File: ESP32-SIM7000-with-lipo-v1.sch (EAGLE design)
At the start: 65 parts, among them IC2 TXB0104, Q1 BSS138L, Q2 BSS138L, Q3 9013, Q5 9013, U3 ESP-WROOM-32, U4 MCP73831T-2ACI/OT, X1 LTE-uFL

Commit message: Naming components
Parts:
- renumbered PGM1 to PROGRAM
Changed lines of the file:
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@@
 <part name="+3V6" library="supply1" library_urn="urn:adsk.eagle:library:371" deviceset="+3V3" device=""/>
 <part name="GND52" library="supply1" library_urn="urn:adsk.eagle:library:371" deviceset="GND" device=""/>
-<part name="PGM1" library="pinhead" deviceset="PINHD-1X6" device=""/>
+<part name="PROGRAM" library="pinhead" deviceset="PINHD-1X6" device=""/>
 <part name="GND3" library="supply1" library_urn="urn:adsk.eagle:library:371" deviceset="GND" device=""/>
 <part name="V2" library="Adafruit111" deviceset="VBUS" device=""/>
@@
 <attribute name="VALUE" x="-78.74" y="-2.54" size="1.778" layer="96"/>
 </instance>
-<instance part="PGM1" gate="A" x="-93.98" y="-63.5" rot="R180">
+<instance part="PROGRAM" gate="A" x="-93.98" y="-63.5" rot="R180">
 <attribute name="NAME" x="-87.63" y="-74.295" size="1.778" layer="95" rot="R180"/>
 <attribute name="VALUE" x="-87.63" y="-53.34" size="1.778" layer="96" rot="R180"/>
@@
 </segment>
 <segment>
-<pinref part="PGM1" gate="A" pin="1"/>
+<pinref part="PROGRAM" gate="A" pin="1"/>
 <wire x1="-91.44" y1="-71.12" x2="-83.82" y2="-71.12" width="0.1524" layer="91"/>
 <pinref part="GND3" gate="1" pin="GND"/>
@@
 </segment>
 <segment>
-<pinref part="PGM1" gate="A" pin="5"/>
+<pinref part="PROGRAM" gate="A" pin="5"/>
 <wire x1="-91.44" y1="-60.96" x2="-78.74" y2="-60.96" width="0.1524" layer="91"/>
 <label x="-78.74" y="-60.96" size="1.27" layer="95" xref="yes"/>
@@
 </segment>
 <segment>
-<pinref part="PGM1" gate="A" pin="6"/>
+<pinref part="PROGRAM" gate="A" pin="6"/>
 <wire x1="-91.44" y1="-58.42" x2="-78.74" y2="-58.42" width="0.1524" layer="91"/>
 <label x="-78.74" y="-58.42" size="1.27" layer="95" xref="yes"/>
@@
 </segment>
 <segment>
-<pinref part="PGM1" gate="A" pin="4"/>
+<pinref part="PROGRAM" gate="A" pin="4"/>
 <wire x1="-91.44" y1="-63.5" x2="-78.74" y2="-63.5" width="0.1524" layer="91"/>
 <label x="-78.74" y="-63.5" size="1.27" layer="95" xref="yes"/>
@@
 </segment>
 <segment>
-<pinref part="PGM1" gate="A" pin="3"/>
+<pinref part="PROGRAM" gate="A" pin="3"/>
 <wire x1="-91.44" y1="-66.04" x2="-78.74" y2="-66.04" width="0.1524" layer="91"/>
 <label x="-78.74" y="-66.04" size="1.27" layer="95" xref="yes"/>
@@
 <net name="VBUS" class="3">
 <segment>
-<pinref part="PGM1" gate="A" pin="2"/>
+<pinref part="PROGRAM" gate="A" pin="2"/>
 <wire x1="-91.44" y1="-68.58" x2="-83.82" y2="-68.58" width="0.1524" layer="91"/>
 <wire x1="-83.82" y1="-68.58" x2="-83.82" y2="-52.07" width="0.1524" layer="91"/>

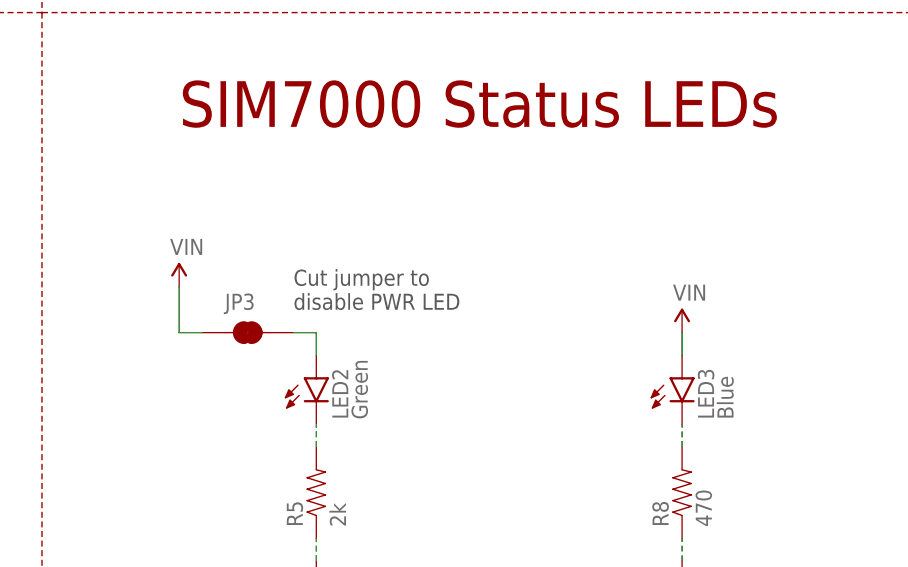
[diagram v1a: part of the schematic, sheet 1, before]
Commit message: adds vias and completes DRC
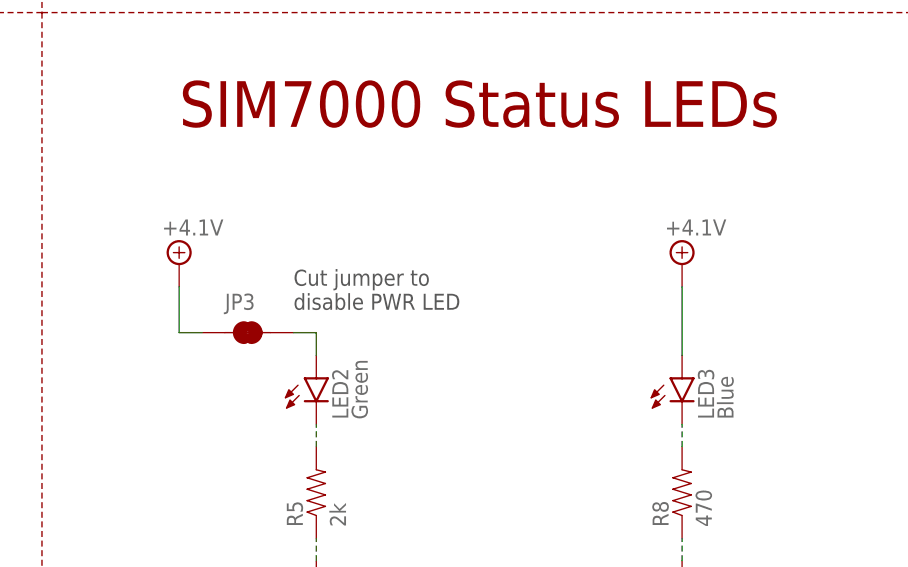
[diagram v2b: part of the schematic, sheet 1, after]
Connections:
- removed net VIN: JP3.1, LED3.A
- net +4.1V: now also JP3.1, LED3.A
- net UC_PWRK: now also U3.IO19
- net UC_RST: now also U3.IO18
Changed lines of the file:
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@@
 <part name="Q1" library="TimWoo-MOSFETs" library_urn="urn:adsk.eagle:library:501962" deviceset="MOSFET-N" device="GENERIC" package3d_urn="urn:adsk.eagle:package:501973/2" value="BSS138L"/>
 <part name="Q2" library="TimWoo-MOSFETs" library_urn="urn:adsk.eagle:library:501962" deviceset="MOSFET-N" device="GENERIC" package3d_urn="urn:adsk.eagle:package:501973/2" value="BSS138L"/>
-<part name="SUPPLY5" library="TimWoo-Aesthetics" library_urn="urn:adsk.eagle:library:502097" deviceset="VIN" device=""/>
-<part name="SUPPLY14" library="TimWoo-Aesthetics" library_urn="urn:adsk.eagle:library:502097" deviceset="VIN" device=""/>
 <part name="JP3" library="TimWoo-Connectors" library_urn="urn:adsk.eagle:library:1036184" deviceset="JUMPER-SMT_2_NC_TRACE" device="_SILK" package3d_urn="urn:adsk.eagle:package:1036528/1"/>
 <part name="GND32" library="SparkFun-Aesthetics" deviceset="GND" device=""/>
@@
 <part name="$H3" library="Adafruit SIM808 Breakout" deviceset="MOUNTINGHOLE" device="3.0THIN"/>
 <part name="$H4" library="Adafruit SIM808 Breakout" deviceset="MOUNTINGHOLE" device="3.0THIN"/>
+<part name="SUPPLY5" library="supply2" library_urn="urn:adsk.eagle:library:372" deviceset="+4.1V" device=""/>
+<part name="SUPPLY8" library="supply2" library_urn="urn:adsk.eagle:library:372" deviceset="+4.1V" device=""/>
 </parts>
 <sheets>
@@
 <attribute name="VALUE" x="210.82" y="31.75" size="1.27" layer="96"/>
 </instance>
-<instance part="SUPPLY5" gate="G$1" x="152.4" y="68.58" smashed="yes">
-<attribute name="VALUE" x="151.384" y="72.136" size="1.778" layer="96"/>
-</instance>
-<instance part="SUPPLY14" gate="G$1" x="208.28" y="63.5" smashed="yes">
-<attribute name="VALUE" x="207.264" y="67.056" size="1.778" layer="96"/>
-</instance>
 <instance part="JP3" gate="G$1" x="160.02" y="63.5" smashed="yes">
 <attribute name="NAME" x="157.48" y="66.04" size="1.778" layer="95"/>
@@
 <instance part="$H3" gate="G$1" x="96.52" y="35.56"/>
 <instance part="$H4" gate="G$1" x="31.75" y="35.56"/>
+<instance part="SUPPLY5" gate="P" x="152.4" y="71.12">
+<attribute name="VALUE" x="150.495" y="74.295" size="1.778" layer="96"/>
+</instance>
+<instance part="SUPPLY8" gate="P" x="208.28" y="71.12">
+<attribute name="VALUE" x="206.375" y="74.295" size="1.778" layer="96"/>
+</instance>
 </instances>
 <busses>
@@
 </segment>
 </net>
-<net name="VIN" class="0">
-<segment>
-<pinref part="LED3" gate="G$1" pin="A"/>
-<pinref part="SUPPLY14" gate="G$1" pin="VIN"/>
-<wire x1="208.28" y1="63.5" x2="208.28" y2="60.96" width="0.1524" layer="91"/>
-</segment>
-<segment>
-<pinref part="JP3" gate="G$1" pin="1"/>
-<wire x1="154.94" y1="63.5" x2="152.4" y2="63.5" width="0.1524" layer="91"/>
-<pinref part="SUPPLY5" gate="G$1" pin="VIN"/>
-<wire x1="152.4" y1="63.5" x2="152.4" y2="68.58" width="0.1524" layer="91"/>
-</segment>
-</net>
 <net name="1.8V" class="0">
 <segment>
@@
 <wire x1="327.66" y1="231.14" x2="327.66" y2="226.06" width="0.1524" layer="91"/>
 <pinref part="SUPPLY2" gate="P" pin="+4.1V"/>
+</segment>
+<segment>
+<pinref part="JP3" gate="G$1" pin="1"/>
+<wire x1="154.94" y1="63.5" x2="152.4" y2="63.5" width="0.1524" layer="91"/>
+<pinref part="SUPPLY5" gate="P" pin="+4.1V"/>
+<wire x1="152.4" y1="63.5" x2="152.4" y2="68.58" width="0.1524" layer="91"/>
+</segment>
+<segment>
+<pinref part="SUPPLY8" gate="P" pin="+4.1V"/>
+<pinref part="LED3" gate="G$1" pin="A"/>
+<wire x1="208.28" y1="68.58" x2="208.28" y2="60.96" width="0.1524" layer="91"/>
 </segment>
 </net>
@@
 <label x="83.82" y="45.72" size="1.27" layer="95" rot="R180" xref="yes"/>
 </segment>
+<segment>
+<pinref part="U3" gate="G$1" pin="IO18"/>
+<wire x1="33.02" y1="-2.54" x2="38.1" y2="-2.54" width="0.1524" layer="91"/>
+<label x="38.1" y="-2.54" size="1.27" layer="95" xref="yes"/>
+</segment>
 </net>
 <net name="UC_PWRK" class="0">
@@
 <label x="83.82" y="53.34" size="1.27" layer="95" rot="R180" xref="yes"/>
 </segment>
-</net>
+<segment>
+<pinref part="U3" gate="G$1" pin="IO19"/>
+<wire x1="33.02" y1="0" x2="38.1" y2="0" width="0.1524" layer="91"/>
+<label x="38.1" y="0" size="1.27" layer="95" xref="yes"/>
+</segment>
+</net>

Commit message: Schematic frames changes
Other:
- moved on the sheet: C13, C14, C15, C16, C17, C21, C5, C7, D4, EN, LIPO, PGM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

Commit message: Logo and config switch
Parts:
- added C10: 0.1uF/16V, rcl:C-EUC0805K
- added R13: 12k, rcl:R-US_M0805
- added SETUP: (no value), special:SW_DIP-1
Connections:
- new net CONFIG: C10.1, R13.1, SETUP.2, U3.IO14
- net +3V3: now also R13.2
- net GND: now also C10.2, SETUP.1
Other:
- note added: "RUN"
- note added: "SETUP"
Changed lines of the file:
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@@
 <part name="SUPPLY8" library="supply2" library_urn="urn:adsk.eagle:library:372" deviceset="+4.1V" device=""/>
 <part name="FRAME3" library="frames" library_urn="urn:adsk.eagle:library:229" deviceset="A4L-LOC" device=""/>
+<part name="SETUP" library="special" deviceset="SW_DIP-1" device=""/>
+<part name="GND30" library="supply1" deviceset="GND" device=""/>
+<part name="C10" library="rcl" deviceset="C-EU" device="C0805K" value="0.1uF/16V"/>
+<part name="R13" library="rcl" deviceset="R-US_" device="M0805" value="12k"/>
+<part name="+3V11" library="supply1" deviceset="+3V3" device=""/>
 </parts>
 <sheets>
@@
 <wire x1="15.24" y1="102.87" x2="15.24" y2="166.37" width="0.1524" layer="95" style="shortdash"/>
 <text x="15.24" y="168.91" size="1.778" layer="95">LIPO CHARGE CONTROLLER</text>
+<text x="289.56" y="93.98" size="1.27" layer="95">RUN</text>
+<text x="289.56" y="107.95" size="1.27" layer="95">SETUP</text>
 </plain>
 <instances>
@@
 </instance>
 <instance part="FRAME3" gate="G$1" x="0" y="0"/>
+<instance part="SETUP" gate="G$1" x="287.02" y="101.6" rot="R270"/>
+<instance part="GND30" gate="1" x="287.02" y="86.36"/>
+<instance part="C10" gate="G$1" x="274.32" y="101.6" smashed="yes">
+<attribute name="NAME" x="275.844" y="101.981" size="1.778" layer="95"/>
+<attribute name="VALUE" x="270.764" y="96.901" size="1.778" layer="96"/>
+</instance>
+<instance part="R13" gate="G$1" x="287.02" y="116.84" rot="R90"/>
+<instance part="+3V11" gate="G$1" x="287.02" y="129.54"/>
 </instances>
 <busses>
@@
 <wire x1="60.96" y1="17.78" x2="60.96" y2="12.7" width="0.1524" layer="91"/>
 </segment>
+<segment>
+<pinref part="SETUP" gate="G$1" pin="1"/>
+<pinref part="GND30" gate="1" pin="GND"/>
+<wire x1="287.02" y1="88.9" x2="287.02" y2="91.44" width="0.1524" layer="91"/>
+<pinref part="C10" gate="G$1" pin="2"/>
+<wire x1="287.02" y1="91.44" x2="287.02" y2="93.98" width="0.1524" layer="91"/>
+<wire x1="274.32" y1="96.52" x2="274.32" y2="91.44" width="0.1524" layer="91"/>
+<wire x1="274.32" y1="91.44" x2="287.02" y2="91.44" width="0.1524" layer="91"/>
+<junction x="287.02" y="91.44"/>
+</segment>
 </net>
 <net name="EN" class="0">
@@
 <pinref part="+3V10" gate="G$1" pin="+3V3"/>
 <wire x1="58.42" y1="25.4" x2="58.42" y2="30.48" width="0.1524" layer="91"/>
+</segment>
+<segment>
+<pinref part="R13" gate="G$1" pin="2"/>
+<pinref part="+3V11" gate="G$1" pin="+3V3"/>
+<wire x1="287.02" y1="127" x2="287.02" y2="121.92" width="0.1524" layer="91"/>
 </segment>
 </net>
@@
 </segment>
 </net>
+<net name="CONFIG" class="0">
+<segment>
+<pinref part="U3" gate="G$1" pin="IO14"/>
+<wire x1="152.4" y1="116.84" x2="144.78" y2="116.84" width="0.1524" layer="91"/>
+<label x="144.78" y="116.84" size="1.27" layer="95" rot="R180" xref="yes"/>
+</segment>
+<segment>
+<pinref part="C10" gate="G$1" pin="1"/>
+<wire x1="274.32" y1="104.14" x2="274.32" y2="111.76" width="0.1524" layer="91"/>
+<pinref part="SETUP" gate="G$1" pin="2"/>
+<wire x1="274.32" y1="111.76" x2="287.02" y2="111.76" width="0.1524" layer="91"/>
+<wire x1="287.02" y1="111.76" x2="287.02" y2="109.22" width="0.1524" layer="91"/>
+<junction x="287.02" y="111.76"/>
+<pinref part="R13" gate="G$1" pin="1"/>
+<wire x1="287.02" y1="111.76" x2="289.56" y2="111.76" width="0.1524" layer="91"/>
+<label x="289.56" y="111.76" size="1.27" layer="95" xref="yes"/>
+</segment>
+</net>

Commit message: Adds TVS and small caps to Vbat pins
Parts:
- added C24: 22uF, SparkFun-Capacitors:22UF-0805-6.3V-20%
- added C25: 33pF, SparkFun-Capacitors:22UF-0805-6.3V-20%
- added C27: 10pF, SparkFun-Capacitors:22UF-0805-6.3V-20%
- added D5: MMSZ5231BT1G, Adafruit SIM808 Breakout:DIODE-ZENERSOD123
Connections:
- removed net LTE_DTR: U1.DTR
- removed net LTE_RI: U1.RI
- removed net UC_DTR: IC2.B4
- removed net UC_RI: IC2.B3
- net +4.1V: now also C24.1, C25.1, C27.1, D5.C
- net GND: now also C24.2, C25.2, C27.2, D5.A
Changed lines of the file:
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@@
 <part name="R13" library="rcl" deviceset="R-US_" device="M0805" value="12k"/>
 <part name="+3V11" library="supply1" deviceset="+3V3" device=""/>
+<part name="D5" library="Adafruit SIM808 Breakout" deviceset="DIODE-ZENER" device="SOD123" value="MMSZ5231BT1G"/>
+<part name="C27" library="SparkFun-Capacitors" deviceset="22UF" device="-0805-6.3V-20%" value="10pF"/>
+<part name="C25" library="SparkFun-Capacitors" deviceset="22UF" device="-0805-6.3V-20%" value="33pF"/>
+<part name="C24" library="SparkFun-Capacitors" deviceset="22UF" device="-0805-6.3V-20%" value="22uF"/>
+<part name="GND47" library="SparkFun" deviceset="GND" device=""/>
+<part name="SUPPLY9" library="supply2" library_urn="urn:adsk.eagle:library:372" deviceset="+4.1V" device=""/>
 </parts>
 <sheets>
@@
 <attribute name="NAME" x="81.28" y="172.085" size="1.778" layer="95" rot="R270"/>
 </instance>
-<instance part="$H1" gate="G$1" x="33.02" y="71.12"/>
-<instance part="$H2" gate="G$1" x="95.25" y="71.12"/>
-<instance part="$H3" gate="G$1" x="96.52" y="35.56"/>
-<instance part="$H4" gate="G$1" x="31.75" y="35.56"/>
+<instance part="$H1" gate="G$1" x="264.16" y="27.94" rot="R90"/>
+<instance part="$H2" gate="G$1" x="265.43" y="12.7"/>
+<instance part="$H3" gate="G$1" x="299.72" y="12.7"/>
+<instance part="$H4" gate="G$1" x="299.72" y="29.21" rot="R90"/>
 <instance part="SUPPLY5" gate="P" x="152.4" y="71.12">
 <attribute name="VALUE" x="150.495" y="74.295" size="1.778" layer="96"/>
@@
 <instance part="SUPPLY8" gate="P" x="208.28" y="71.12">
 <attribute name="VALUE" x="206.375" y="74.295" size="1.778" layer="96"/>
+</instance>
+<instance part="D5" gate="G$1" x="82.55" y="44.45" rot="R90"/>
+<instance part="C27" gate="G$1" x="71.12" y="43.18"/>
+<instance part="C25" gate="G$1" x="62.23" y="43.18"/>
+<instance part="C24" gate="G$1" x="50.8" y="43.18"/>
+<instance part="GND47" gate="1" x="67.31" y="27.94" rot="MR0"/>
+<instance part="SUPPLY9" gate="P" x="66.04" y="60.96">
+<attribute name="VALUE" x="64.135" y="64.135" size="1.778" layer="96"/>
 </instance>
 </instances>
@@
 <junction x="194.31" y="138.43"/>
 </segment>
+<segment>
+<pinref part="C24" gate="G$1" pin="2"/>
+<wire x1="50.8" y1="40.64" x2="50.8" y2="36.83" width="0.1524" layer="91"/>
+<wire x1="50.8" y1="36.83" x2="62.23" y2="36.83" width="0.1524" layer="91"/>
+<pinref part="D5" gate="G$1" pin="A"/>
+<wire x1="62.23" y1="36.83" x2="67.31" y2="36.83" width="0.1524" layer="91"/>
+<wire x1="67.31" y1="36.83" x2="71.12" y2="36.83" width="0.1524" layer="91"/>
+<wire x1="71.12" y1="36.83" x2="82.55" y2="36.83" width="0.1524" layer="91"/>
+<wire x1="82.55" y1="36.83" x2="82.55" y2="41.91" width="0.1524" layer="91"/>
+<pinref part="C27" gate="G$1" pin="2"/>
+<wire x1="71.12" y1="40.64" x2="71.12" y2="36.83" width="0.1524" layer="91"/>
+<junction x="71.12" y="36.83"/>
+<pinref part="C25" gate="G$1" pin="2"/>
+<wire x1="62.23" y1="40.64" x2="62.23" y2="36.83" width="0.1524" layer="91"/>
+<junction x="62.23" y="36.83"/>
+<pinref part="GND47" gate="1" pin="GND"/>
+<wire x1="67.31" y1="30.48" x2="67.31" y2="36.83" width="0.1524" layer="91"/>
+<junction x="67.31" y="36.83"/>
+</segment>
 </net>
 <net name="1.8V" class="0">
@@
 </segment>
 </net>
-<net name="LTE_RI" class="0">
-<segment>
-<pinref part="U1" gate="G$1" pin="RI"/>
-<wire x1="281.94" y1="195.58" x2="279.4" y2="195.58" width="0.1524" layer="91"/>
-<label x="279.4" y="195.58" size="1.27" layer="95" rot="R180" xref="yes"/>
-</segment>
-</net>
 <net name="LTE_RXD" class="0">
 <segment>
@@
 </segment>
 </net>
-<net name="UC_RI" class="0">
-<segment>
-<pinref part="IC2" gate="G$1" pin="B3"/>
-<wire x1="190.5" y1="215.9" x2="193.04" y2="215.9" width="0.1524" layer="91"/>
-<label x="193.04" y="215.9" size="1.27" layer="95" xref="yes"/>
-</segment>
-</net>
 <net name="N$4" class="0">
 <segment>
@@
 <pinref part="LED3" gate="G$1" pin="C"/>
 <wire x1="208.28" y1="50.8" x2="208.28" y2="53.34" width="0.1524" layer="91" style="longdash"/>
-</segment>
-</net>
-<net name="LTE_DTR" class="0">
-<segment>
-<pinref part="U1" gate="G$1" pin="DTR"/>
-<wire x1="281.94" y1="198.12" x2="271.78" y2="198.12" width="0.1524" layer="91"/>
-<label x="271.78" y="198.12" size="1.27" layer="95" rot="R180" xref="yes"/>
-</segment>
-</net>
-<net name="UC_DTR" class="0">
-<segment>
-<pinref part="IC2" gate="G$1" pin="B4"/>
-<wire x1="190.5" y1="213.36" x2="193.04" y2="213.36" width="0.1524" layer="91"/>
-<label x="193.04" y="213.36" size="1.27" layer="95" xref="yes"/>
 </segment>
 </net>
@@
 <wire x1="208.28" y1="68.58" x2="208.28" y2="60.96" width="0.1524" layer="91"/>
 </segment>
-</net>
+<segment>
+<pinref part="D5" gate="G$1" pin="C"/>
+<wire x1="82.55" y1="46.99" x2="82.55" y2="53.34" width="0.1524" layer="91"/>
+<wire x1="82.55" y1="53.34" x2="71.12" y2="53.34" width="0.1524" layer="91"/>
+<pinref part="C24" gate="G$1" pin="1"/>
+<wire x1="71.12" y1="53.34" x2="66.04" y2="53.34" width="0.1524" layer="91"/>
+<wire x1="66.04" y1="53.34" x2="62.23" y2="53.34" width="0.1524" layer="91"/>
+<wire x1="62.23" y1="53.34" x2="50.8" y2="53.34" width="0.1524" layer="91"/>
+<wire x1="50.8" y1="53.34" x2="50.8" y2="48.26" width="0.1524" layer="91"/>
+<pinref part="C25" gate="G$1" pin="1"/>
+<wire x1="62.23" y1="48.26" x2="62.23" y2="53.34" width="0.1524" layer="91"/>
+<junction x="62.23" y="53.34"/>
+<pinref part="C27" gate="G$1" pin="1"/>
+<wire x1="71.12" y1="48.26" x2="71.12" y2="53.34" width="0.1524" layer="91"/>
+<junction x="71.12" y="53.34"/>
+<wire x1="66.04" y1="58.42" x2="66.04" y2="53.34" width="0.1524" layer="91"/>
+<junction x="66.04" y="53.34"/>
+<pinref part="SUPPLY9" gate="P" pin="+4.1V"/>
+</segment>
+</net>
